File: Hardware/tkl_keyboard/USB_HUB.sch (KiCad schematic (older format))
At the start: 21 parts, among them U4 TUSB2046b, U6 SRV05-4, U8 SRV05-4, X1 625L3C006M00000

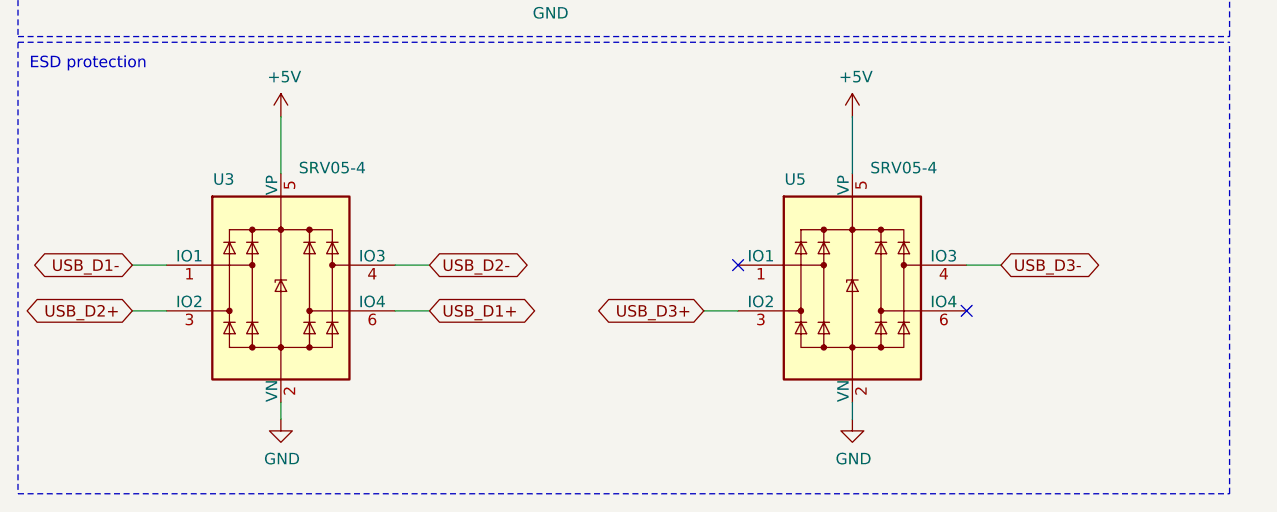
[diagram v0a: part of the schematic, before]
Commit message: LEDs and diodes routed
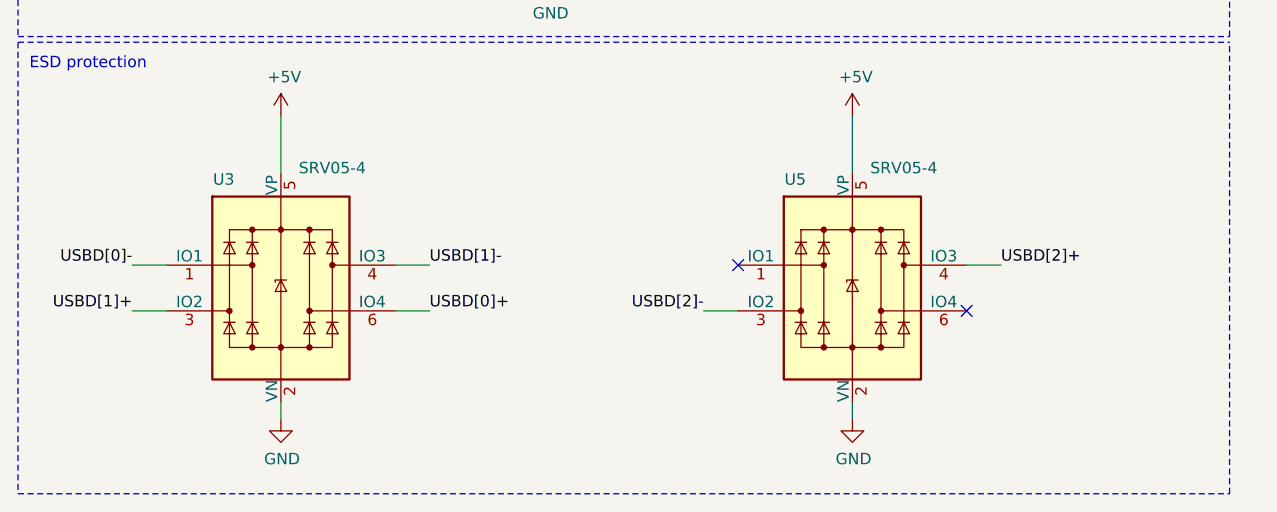
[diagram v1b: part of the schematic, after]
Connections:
- net USB_D1+ is gone; now on net USBD[0]+: U6.6 (IO4)
- net USB_D1- is gone; now on net USBD[0]-: U6.1 (IO1)
- net USB_D2+ is gone; now on net USBD[1]+: U6.3 (IO2)
- net USB_D2- is gone; now on net USBD[1]-: U6.4 (IO3)
- net USB_D3+ is gone; now on net USBD[2]-: U8.3 (IO2)
- net USB_D3- is gone; now on net USBD[2]+: U8.4 (IO3)
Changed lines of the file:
@@
 Wire Wire Line
 	4800 6550 4950 6550
-Wire Wire Line
-	3800 6750 3650 6750
 $Comp
 L custom_parts_library:625L3C006M00000 X1
@@
 Wire Wire Line
 	3075 2100 3075 2225
-Text GLabel 2450 6750 2    50   BiDi ~ 0
-USB_D1+
-Text GLabel 1150 6550 0    50   BiDi ~ 0
-USB_D1-
-Text GLabel 2450 6550 2    50   BiDi ~ 0
-USB_D2-
-Text GLabel 3650 6750 0    50   BiDi ~ 0
-USB_D3+
-Text GLabel 4950 6550 2    50   BiDi ~ 0
-USB_D3-
 $Comp
 L Power_Protection:SRV05-4 U?
@@
 Wire Wire Line
 	1300 6750 1150 6750
-Text GLabel 1150 6750 0    50   BiDi ~ 0
-USB_D2+
 Wire Notes Line
 	650  5575 650  7550
@@
 Wire Notes Line
 	8575 1275 5975 1275
+Text Label 4950 6550 0    50   ~ 0
+USBD[2]+
+Wire Wire Line
+	3800 6750 3650 6750
+Text Label 3650 6750 2    50   ~ 0
+USBD[2]-
+Text Label 2450 6550 0    50   ~ 0
+USBD[1]-
+Text Label 2450 6750 0    50   ~ 0
+USBD[0]+
+Text Label 1150 6550 2    50   ~ 0
+USBD[0]-
+Text Label 1150 6750 2    50   ~ 0
+USBD[1]+
 $EndSCHEMATC

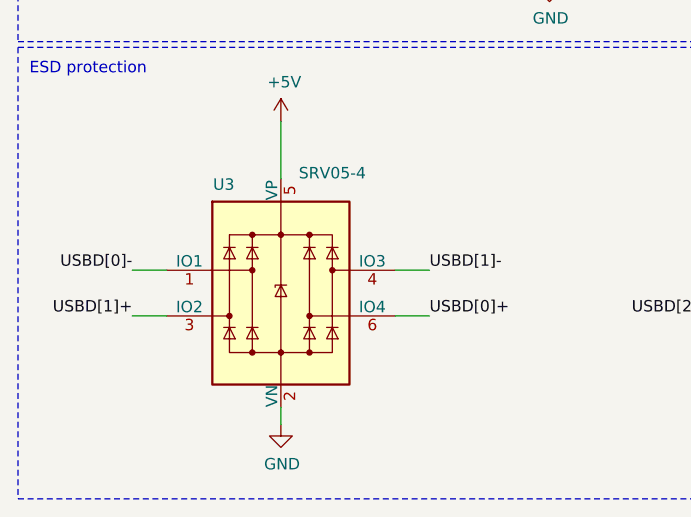
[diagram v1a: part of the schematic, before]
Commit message: Rows and columns routed to controller. Extended top board edge to fit OLED. Removed optional resistors around CMC.
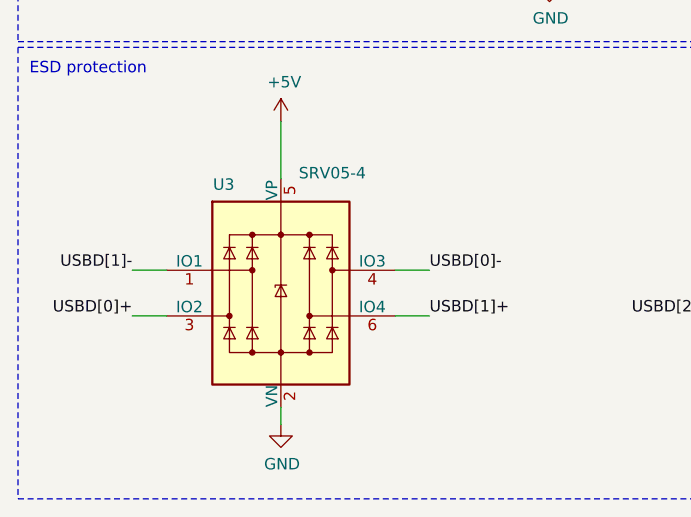
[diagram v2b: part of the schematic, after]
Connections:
- net USBD[0]+: now also U6.3 (IO2); no longer U6.6 (IO4)
- net USBD[0]-: now also U6.4 (IO3); no longer U6.1 (IO1)
- net USBD[1]+: now also U6.6 (IO4); no longer U6.3 (IO2)
- net USBD[1]-: now also U6.1 (IO1); no longer U6.4 (IO3)
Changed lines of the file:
@@
 	4300 7225 4300 7150
 Wire Wire Line
+	2300 6550 2450 6550
+Wire Wire Line
+	1300 6750 1150 6750
+Wire Wire Line
 	1300 6550 1150 6550
-Wire Wire Line
-	2300 6750 2450 6750
-Wire Wire Line
-	2300 6550 2450 6550
 Wire Wire Line
 	4800 6550 4950 6550
@@
 $EndComp
 Wire Wire Line
-	1300 6750 1150 6750
+	2300 6750 2450 6750
 Wire Notes Line
 	650  5575 650  7550
@@
 Text Label 3650 6750 2    50   ~ 0
 USBD[2]-
+Text Label 1150 6550 2    50   ~ 0
+USBD[1]-
+Text Label 1150 6750 2    50   ~ 0
+USBD[0]+
 Text Label 2450 6550 0    50   ~ 0
-USBD[1]-
+USBD[0]-
 Text Label 2450 6750 0    50   ~ 0
-USBD[0]+
-Text Label 1150 6550 2    50   ~ 0
-USBD[0]-
-Text Label 1150 6750 2    50   ~ 0
 USBD[1]+
 $EndSCHEMATC

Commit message: Updating schematic
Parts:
- R10, R9: value 4K7 -> 10K
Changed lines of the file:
@@
 $Descr A4 11693 8268
 encoding utf-8
-Sheet 2 11
+Sheet 2 12
 Title ""
 Date ""
@@
 AR Path="/62FAC6FD/624972FE" Ref="R8"  Part="1"
 F 0 "R8" V 1350 3875 50  0000 C CNN
-F 1 "4K7" V 1250 3875 50  0000 C CNN
+F 1 "10K" V 1250 3875 50  0000 C CNN
 F 2 "resistor_smd:R_0603_1608Metric" V 1180 3875 50  0001 C CNN
 F 3 "~" H 1250 3875 50  0001 C CNN
@@
 AR Path="/62FAC6FD/6249730E" Ref="R9"  Part="1"
 F 0 "R9" V 1750 4450 50  0000 C CNN
-F 1 "4K7" V 1650 4450 50  0000 C CNN
+F 1 "10K" V 1650 4450 50  0000 C CNN
 F 2 "resistor_smd:R_0603_1608Metric" V 1580 4450 50  0001 C CNN
 F 3 "~" H 1650 4450 50  0001 C CNN

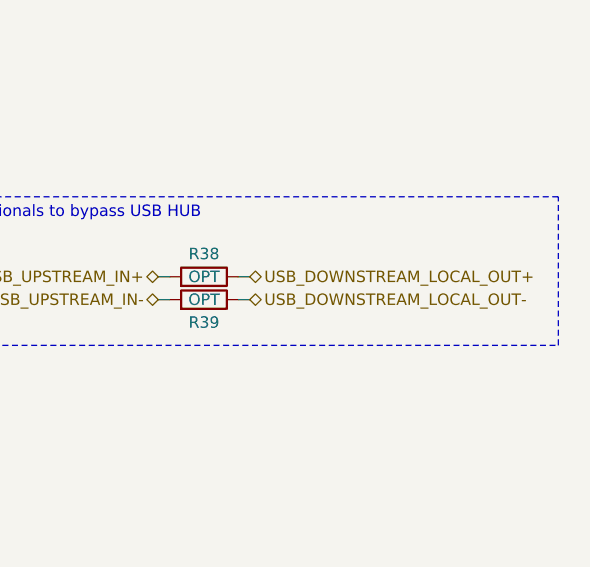
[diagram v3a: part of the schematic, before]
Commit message: First pass of routing done
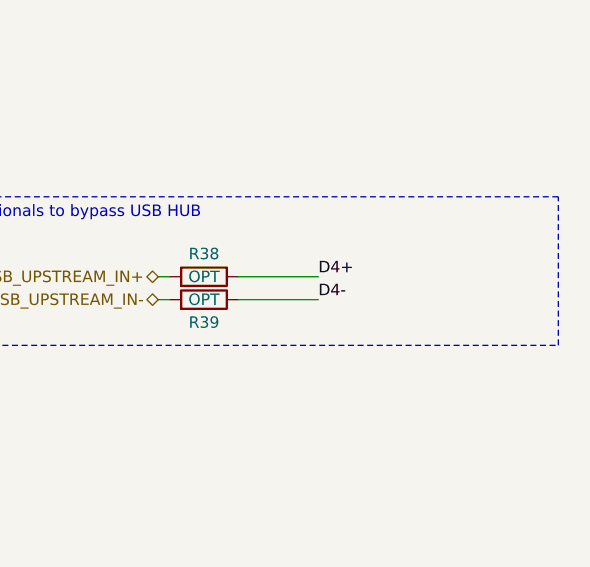
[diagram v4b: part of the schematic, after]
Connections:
- net D4+: now also R38.1
- net D4-: now also R39.1
- net USB_DOWNSTREAM_LOCAL_OUT+: no longer R38.1
- net USB_DOWNSTREAM_LOCAL_OUT-: no longer R39.1
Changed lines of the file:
@@
 Text HLabel 6825 1725 0    50   BiDi ~ 0
 USB_UPSTREAM_IN-
-Text HLabel 7225 1625 2    50   BiDi ~ 0
-USB_DOWNSTREAM_LOCAL_OUT+
-Text HLabel 7225 1725 2    50   BiDi ~ 0
-USB_DOWNSTREAM_LOCAL_OUT-
 $Comp
 L Device:R R?
@@
 Wire Wire Line
 	6875 1625 6825 1625
-Wire Wire Line
-	7175 1625 7225 1625
-Wire Wire Line
-	7175 1725 7225 1725
 Wire Wire Line
 	6875 1725 6825 1725
@@
 Text Label 2450 6750 0    50   ~ 0
 USBD[1]+
+Wire Wire Line
+	7175 1625 7525 1625
+Wire Wire Line
+	7175 1725 7525 1725
+Text Label 7525 1625 0    50   ~ 0
+D4+
+Text Label 7525 1725 0    50   ~ 0
+D4-
 $EndSCHEMATC

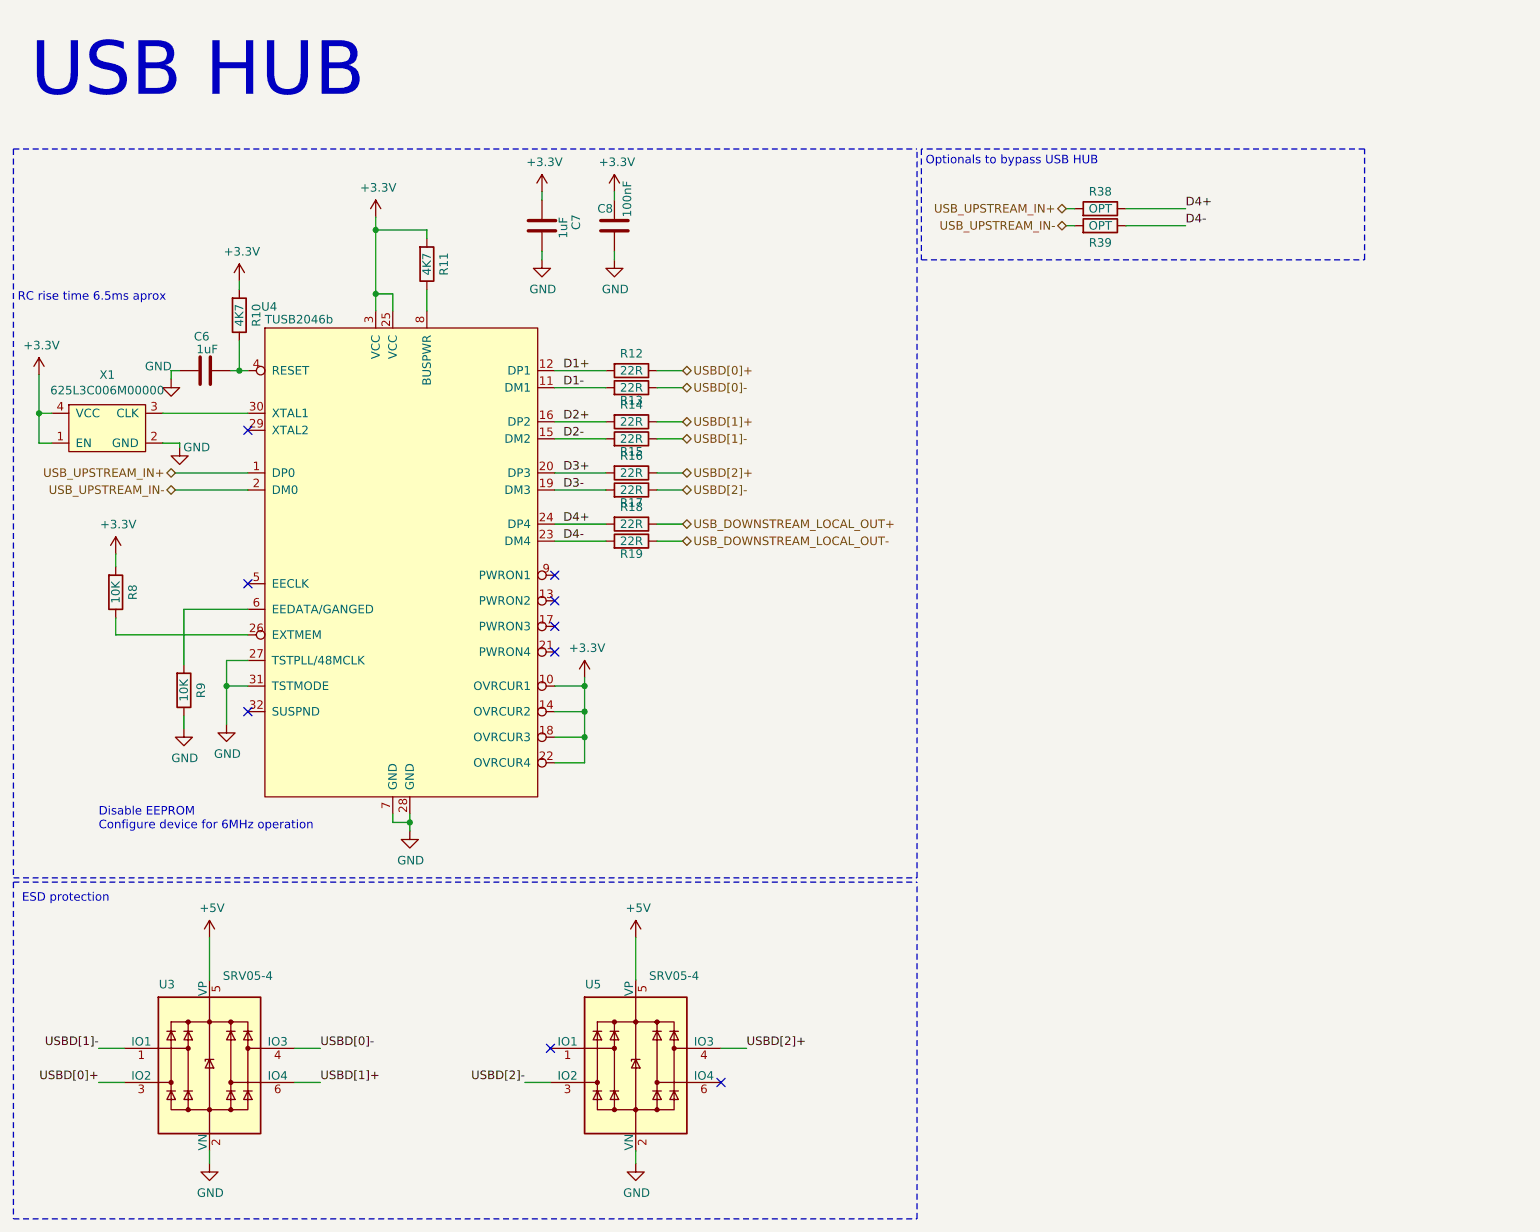
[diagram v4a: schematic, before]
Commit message: Tidying schematic
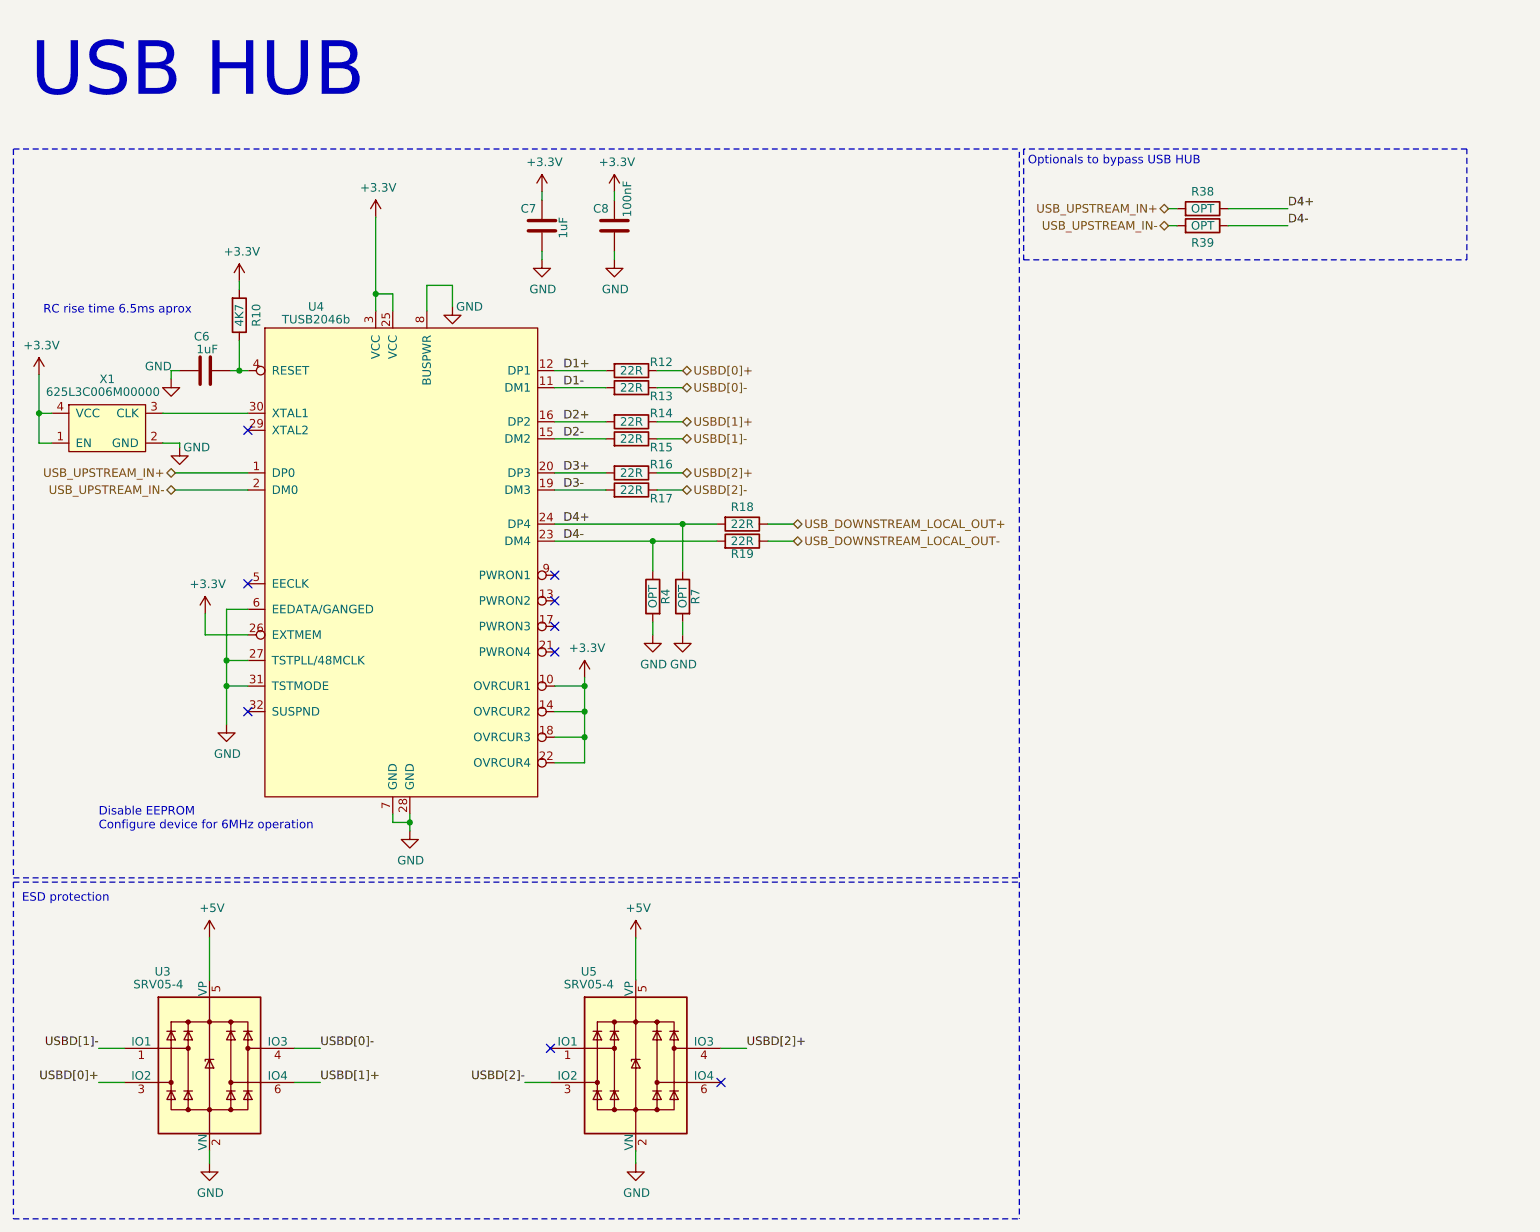
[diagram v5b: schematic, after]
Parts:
- removed R10, R9: 10K, resistor_smd:R_0603_1608Metric, symbol Device:R
- removed R11: 4K7, resistor_smd:R_0603_1608Metric, symbol Device:R
- added R4, R7: OPT, resistor_smd:R_0603_1608Metric, symbol Device:R
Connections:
- net +3V3: now also U4.26 (EXTMEM)
- net D4+: now also R7.1
- net D4-: now also R4.1
- net GND: now also U4.6 (EEDATA/GANGED), U4.8 (BUSPWR), R4.2, R7.2
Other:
- moved on the sheet: R18, R19, R38, R39

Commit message: Generating gerbers
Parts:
- added R8: OPT, resistor_smd:R_0603_1608Metric, symbol Device:R
- added U10: 74AHC1G17, Package_TO_SOT_SMD:SOT-353_SC-70-5, symbol custom_parts_library:74AHC1G17
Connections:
- net +3V3: now also U10.5
- net GND: now also U10.3
- net at C44.2, R1.1: now also R8.1, U10.2; no longer U4.4 (RESET)
- new net: R8.2, U10.4, U4.4 (RESET)
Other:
- moved on the sheet: C6, C7, C8, R10, R12, R13, R14, R15, R16, R17, R18, R19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
